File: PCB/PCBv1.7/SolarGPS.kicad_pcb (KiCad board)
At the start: 2 copper layers, 80 x 30 mm, 38 parts, among them J1 Conn_01x10_Female, J2 GND, J3 GND, J4 Solar1+, J5 Solar2+, J6 Conn_02x03_Odd_Even, J7 Screw_Terminal_01x01, J8 Conn_01x04_Male, SW1 SW_Push, U1 TPS63802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

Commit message: Submit board 1.7
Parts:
- removed D2: Schottky, Diode_SMD:D_SOD-323_HandSoldering
- added U5: LM66100, Package_TO_SOT_SMD:SOT-363_SC-70-6, F.Cu at (77.3, 55.0)
- added U6: LM66100, Package_TO_SOT_SMD:SOT-363_SC-70-6, F.Cu at (77.3, 52.1)
- D1: value Schottky -> 4V; footprint Diode_SMD:D_SOD-323_HandSoldering -> Diode_SMD:D_SMB_Handsoldering; moved to B.Cu
- U4: value MAX40200AUK -> LM66100; footprint Package_TO_SOT_SMD:SOT-23-5 -> Package_TO_SOT_SMD:SOT-363_SC-70-6
- moved D1 13.0 mm to (66.2, 61.5), turned to 90 degrees
- moved C10 1.88 mm to (73.0, 55.1)
- moved R4 0.72 mm to (116.0, 76.8)
- moved U4 0.30 mm to (116.0, 74.6)
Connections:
- net /VBAT renamed VBAT
- D1 pad 2: /SOLAR1+ -> GND
- U4 pad 5: /GPS_VDD -> GND
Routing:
- net VBAT: track 30.1 -> 46.4 mm
- net GND: vias 54 -> 55

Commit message: Tweak PCB
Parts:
- removed D1: 4V, Diode_SMD:D_SMB_Handsoldering
- removed R4: 432k, Resistor_SMD:R_0603_1608Metric
- removed SW1: SW_Push, Button_Switch_SMD:SW_SPST_CK_RS282G05A3
- added C11: 1uF, Capacitor_SMD:C_0603_1608Metric, F.Cu at (78.0, 70.9)
- added D3: LED_Small, Diode_SMD:D_0805_2012Metric, F.Cu at (57.3, 57.2)
- added R5: 60, Resistor_SMD:R_0603_1608Metric, F.Cu at (60.6, 57.5)
- added U7: MAX40200AUK, Package_TO_SOT_SMD:SOT-23-5, F.Cu at (107.3, 99.8)
- C7: value 0.1uF -> 1uF
- R1: value 100 -> 86k
- U4: value LM66100 -> BMI160; footprint Package_TO_SOT_SMD:SOT-363_SC-70-6 -> digikey-footprints:BMI160
- U5, U6: value LM66100 -> MAX40200AUK; footprint Package_TO_SOT_SMD:SOT-363_SC-70-6 -> Package_TO_SOT_SMD:SOT-23-5
- moved U6 60.1 mm to (107.3, 104.2), turned to 0 degrees
- moved U5 56.9 mm to (112.5, 99.8), turned to 0 degrees
- moved U4 38.8 mm to (77.2, 73.5), turned to 90 degrees
- moved C16 3.03 mm to (73.0, 69.3), turned to 90 degrees
- moved C1 1.05 mm to (118.8, 74.1)
- moved C5 0.98 mm to (119.0, 75.9)
- moved R6 0.25 mm to (63.8, 57.5)
- moved C7 0.20 mm to (63.5, 51.5)
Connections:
- C10 pad 2: VBAT -> /VBAT
- C4 pad 1: VBAT -> /VBAT
- C6 pad 2: VBAT -> /VBAT
- R2 pad 1: VBAT -> /VBAT
- U1 pad 10: VBAT -> /VBAT
- U3 pad 14: unconnected-(U3-Pad14) -> MMU_INT
- U3 pad 15: unconnected-(U3-Pad15) -> MMU_CS
- U3 pad 18: LCDEN -> SOLAREN
- U3 pad 19: DISPCS -> LCDEN
- U3 pad 20: unconnected-(U3-Pad20) -> DISPCS
- U3 pad 22: unconnected-(U3-Pad22) -> LED
- U3 pad 6: Button -> unconnected-(U3-Pad6)
- U4 pad 1: VDD -> SPI_MISO
- U4 pad 2: GND -> unconnected-(U4-Pad2)
- U4 pad 3: GPS_EN -> unconnected-(U4-Pad3)
- U4 pad 4: unconnected-(U4-Pad4) -> MMU_INT
- U4 pad 5: GND -> VDD
- U4 pad 6: /GPS_VDD -> GND
- U5 pad 1: /SOLAR1+ -> VDD
- U5 pad 3: VBAT -> GPS_EN
- U5 pad 5: GND -> /GPS_VDD
- U6 pad 1: /SOLAR2+ -> /SOLAR1+
- U6 pad 3: VBAT -> SOLAREN
- U6 pad 5: GND -> /VBAT
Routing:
- net VBAT: track 46.4 -> 0.00 mm, vias 1 -> 0
- net /VBAT: track 0.00 -> 36.4 mm, vias 0 -> 1
- net Button: track 28.3 -> 0.00 mm, vias 2 -> 0
- net LED: track 0.00 -> 20.9 mm
- net VDD: track 145.4 -> 164.6 mm, vias 3 -> 2
- net /GPS_VDD: track 17.6 -> 0.00 mm
- net MMU_INT: track 0.00 -> 13.0 mm, vias 0 -> 2
- net GPS_EN: track 47.5 -> 59.4 mm, vias 1 -> 3
- net SPI_CLK: track 15.7 -> 19.7 mm, vias 2 -> 3
- net MMU_CS: track 0.00 -> 3.97 mm
- net SPI_MISO: track 0.00 -> 3.96 mm
- net GND: track 7.95 -> 11.8 mm, vias 55 -> 59
- net SPI_MOSI: track 17.5 -> 19.7 mm
- net Net-(D3-Pad2): track 0.00 -> 1.69 mm

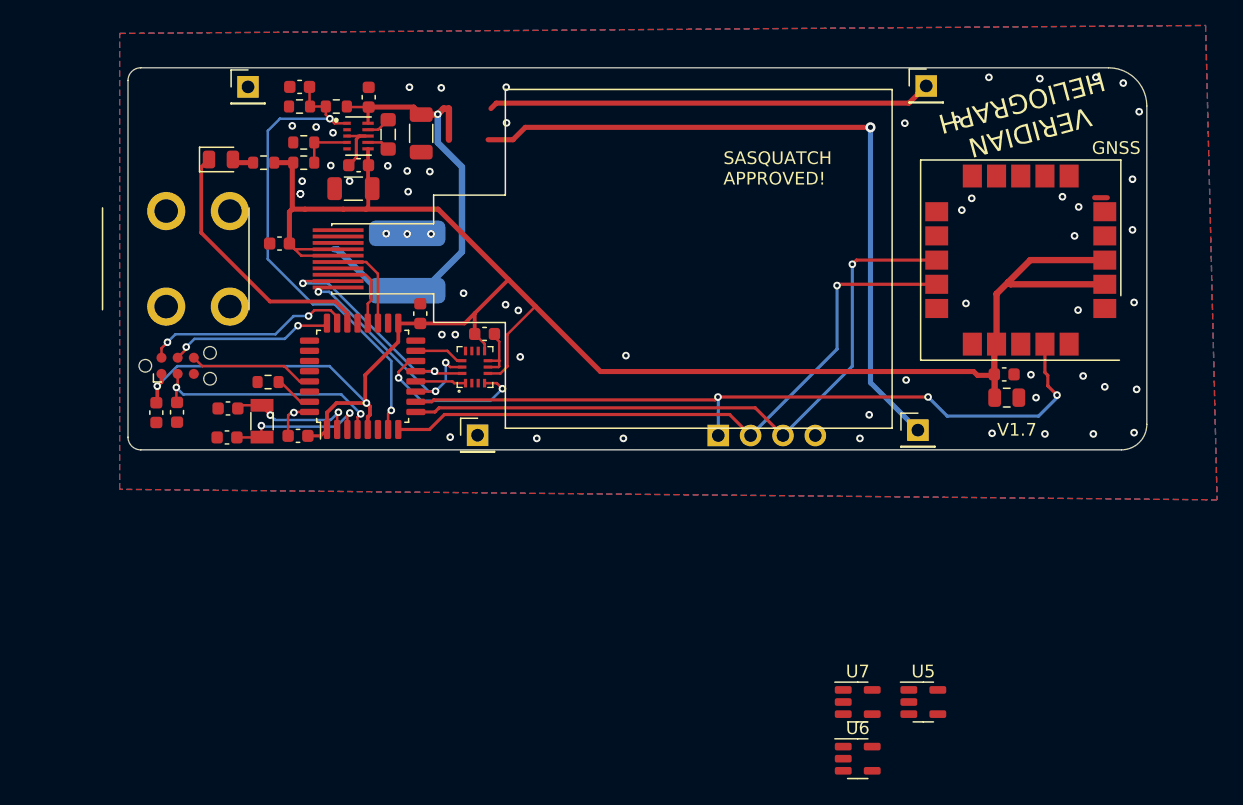
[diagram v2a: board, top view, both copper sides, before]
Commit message: add USB!
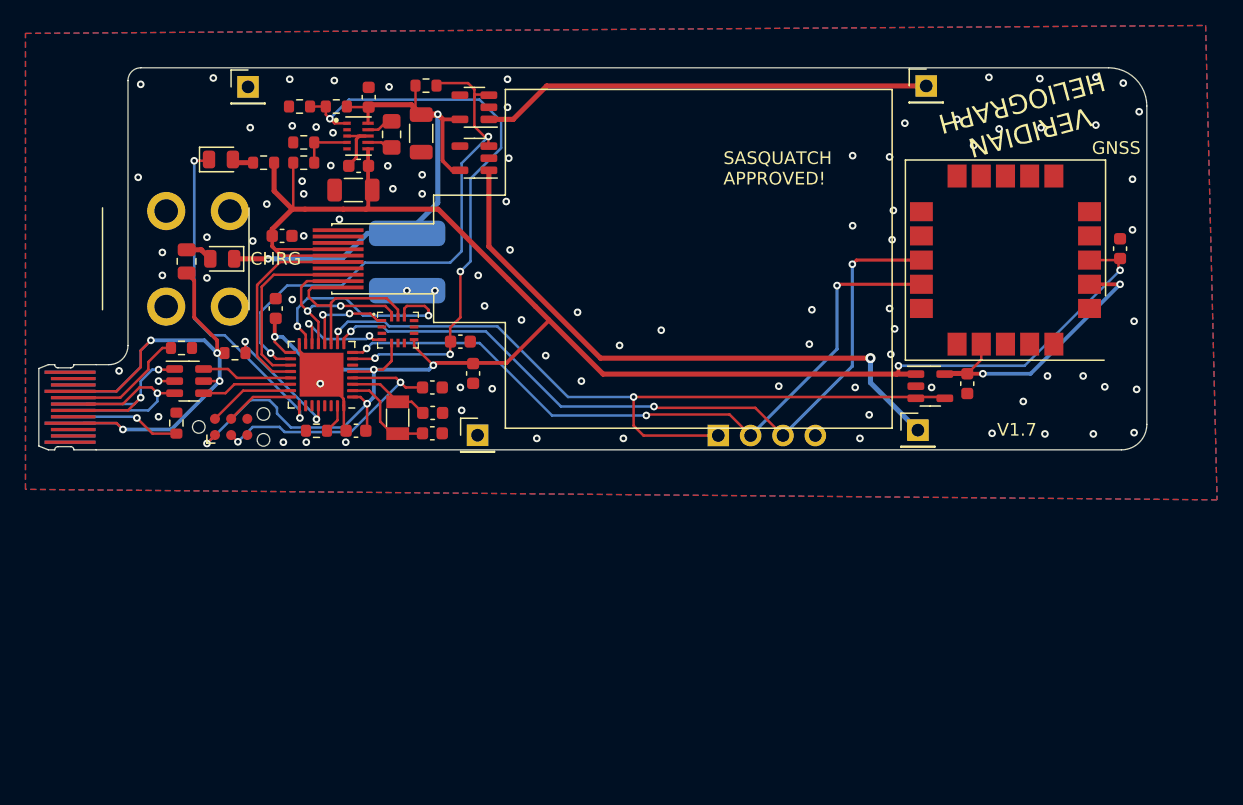
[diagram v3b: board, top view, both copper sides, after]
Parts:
- removed C11, C19: 1uF, Capacitor_SMD:C_0603_1608Metric
- removed C5: 4.7uF, Capacitor_SMD:C_0805_2012Metric
- added C12: 1uF, Capacitor_SMD:C_0603_1608Metric, F.Cu at (127.9, 64.2)
- added C17: 1uF, Capacitor_SMD:C_0603_1608Metric, F.Cu at (77.1, 74.0)
- added D1: LED_Small, Diode_SMD:D_0805_2012Metric, F.Cu at (57.4, 65.0)
- added J9: USB_C_Receptacle_USB2.0, Veridian:USB_TYPE_C_PCB, F.Cu at (43.0, 76.7)
- added R10: 10, Resistor_SMD:R_0805_2012Metric, F.Cu at (54.6, 65.2)
- added R11: 5.1K, Resistor_SMD:R_0603_1608Metric, F.Cu at (58.4, 72.4)
- added R4: 86k, Resistor_SMD:R_0603_1608Metric, F.Cu at (73.4, 51.4)
- added R8: 5.1K, Resistor_SMD:R_0603_1608Metric, F.Cu at (54.2, 72.0)
- added R9: 5.1K, Resistor_SMD:R_0603_1608Metric, F.Cu at (53.8, 77.9)
- added U8: USBLC6-2SC6, Package_TO_SOT_SMD:SOT-23-6, F.Cu at (54.8, 74.6)
- C10, C9: value 47uF -> 22uF
- C8: value 10nF -> 1uF
- L1: footprint Inductor_SMD:L_0805_2012Metric_Pad1.05x1.20mm_HandSolder -> Inductor_SMD:L_0805_2012Metric_Pad1.15x1.40mm_HandSolder
- U3: value STM32L071KBTx -> STM32L432KCUx; footprint Package_QFP:LQFP-32_7x7mm_P0.8mm -> Package_DFN_QFN:QFN-32-1EP_5x5mm_P0.5mm_EP3.45x3.45mm
- moved U6 55.9 mm to (77.2, 57.1), turned to 180 degrees
- moved U7 55.6 mm to (77.2, 53.1), turned to 180 degrees
- moved U5 24.8 mm to (113.0, 75.0)
- moved C7 23.6 mm to (76.1, 71.5), turned to 180 degrees
- moved C2 20.1 mm to (73.9, 75.1), turned to 0 degrees
- moved C13 16.3 mm to (73.9, 77.1), turned to 0 degrees
- moved C15 16.2 mm to (73.9, 78.7), turned to 0 degrees
- moved Y1 10.7 mm to (71.2, 77.5), turned to -90 degrees
- moved C16 10.5 mm to (67.9, 78.5), turned to 180 degrees
- moved C14 10.2 mm to (61.6, 68.9), turned to 90 degrees
- moved U4 6.71 mm to (71.2, 70.6), turned to 0 degrees
- moved J6 6.38 mm to (58.1, 78.2)
- moved R1 5.39 mm to (64.8, 78.5)
- moved U3 3.23 mm to (65.2, 74.1), turned to 180 degrees
- moved C1 2.99 mm to (115.9, 74.8), turned to 90 degrees
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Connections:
- net /VBAT renamed VBAT
- J6 pad 6: UART1TX -> unconnected-(J6-Pad6)
- U3 pad 19: LCDEN -> DISPCS
- U3 pad 20: DISPCS -> LCDEN
- U3 pad 21: unconnected-(U3-Pad21) -> USB_N
- U3 pad 22: LED -> USB_P
- U3 pad 25: unconnected-(U3-Pad25) -> LED
- U3 pad 28: unconnected-(U3-Pad28) -> Net-(U3-Pad28)
- U3 pad 29: UART1TX -> unconnected-(U3-Pad29)
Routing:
- net VUSB: track 0.00 -> 49.4 mm, vias 0 -> 4
- net SOLAREN: track 0.00 -> 42.6 mm, vias 0 -> 2
- net /GPS_VDD: track 0.00 -> 21.8 mm, vias 0 -> 2
- net USBR_P: track 0.00 -> 14.2 mm, vias 0 -> 1
- net USBR_N: track 0.00 -> 13.6 mm, vias 0 -> 2
- net MMU_CS: track 3.97 -> 17.5 mm, vias 0 -> 2
- net Net-(U3-Pad28): track 0.00 -> 10.5 mm, vias 0 -> 2
- net UART1TX: track 9.85 -> 0.00 mm
- net SWDIO: track 16.5 -> 6.85 mm, vias 2 -> 0
- net /SOLAR1+: track 55.7 -> 46.8 mm
- net Net-(J9-PadA5): track 0.00 -> 8.64 mm
- net LCDEN: track 7.38 -> 15.8 mm
- net DISPCS: track 6.26 -> 14.3 mm
- net GPS_UART_MISO: track 52.3 -> 60.1 mm, vias 1 -> 3
- net Net-(J9-PadB5): track 0.00 -> 7.65 mm, vias 0 -> 1
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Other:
- board size 80 x 30 mm -> 82.5 x 30 mm
- board text added: "CHRG"

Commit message: Add USB pulldown and SWO
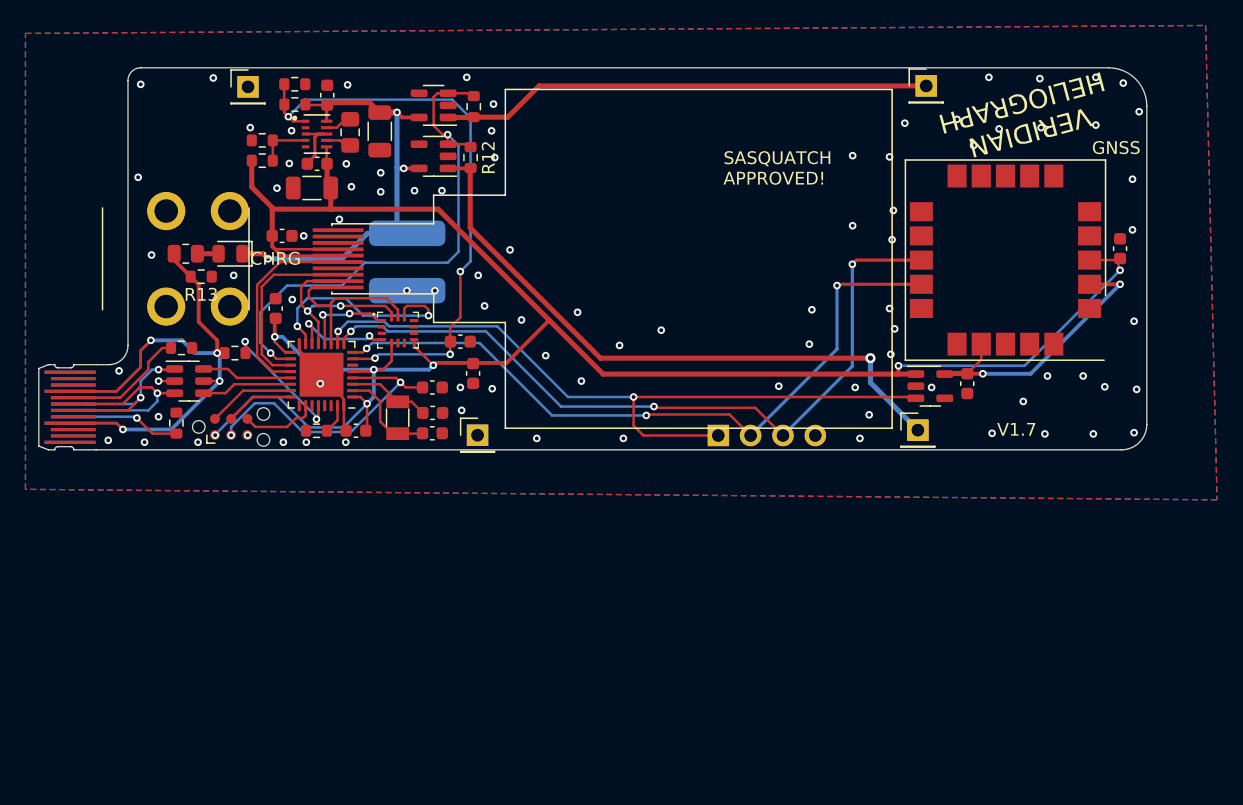
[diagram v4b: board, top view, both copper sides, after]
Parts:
- removed D3: LED_Small, Diode_SMD:D_0805_2012Metric
- removed R5: 60, Resistor_SMD:R_0603_1608Metric
- added R12: 86k, Resistor_SMD:R_0603_1608Metric, F.Cu at (76.9, 57.0)
- added R13: 5.1K, Resistor_SMD:R_0603_1608Metric, F.Cu at (55.8, 66.4)
- moved R4 4.10 mm to (77.2, 53.0), turned to -90 degrees
- moved C6 3.26 mm to (65.6, 52.1)
- moved C9 3.26 mm to (64.4, 59.4)
- moved C10 3.26 mm to (69.8, 55.0)
- moved L1 3.26 mm to (67.4, 55.1)
- moved R2 3.26 mm to (63.1, 52.9)
- moved C8 3.26 mm to (64.9, 57.5)
- moved R6 3.26 mm to (60.5, 57.3)
- moved R7 3.26 mm to (60.5, 55.7)
- moved U1 3.26 mm to (64.8, 55.2)
- moved U6 3.20 mm to (74.0, 57.0)
- moved U7 3.20 mm to (74.0, 53.0)
- moved R3 1.79 mm to (63.1, 51.3), turned to 0 degrees
- moved D1 0.76 mm to (58.0, 64.6)
- moved R10 0.60 mm to (54.5, 64.6), turned to 0 degrees
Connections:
- J6 pad 6: unconnected-(J6-Pad6) -> SWO
- R4 pad 2: VBAT -> /SOLAR2+
- U3 pad 26: unconnected-(U3-Pad26) -> SWO
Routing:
- net LED: track 26.5 -> 0.00 mm, vias 2 -> 0
- net VBAT: track 43.4 -> 36.8 mm, vias 2 -> 3
- net SWO: track 0.00 -> 5.98 mm
- net VDD: track 164.1 -> 159.9 mm
- net /SOLAR2+: track 35.4 -> 38.5 mm
- net GPS_EN: track 61.0 -> 58.4 mm
- net /SOLAR1+: track 46.8 -> 49.3 mm
- net VUSB: track 49.4 -> 51.4 mm
- net Net-(D3-Pad2): track 1.69 -> 0.00 mm
- net nRESET: track 21.6 -> 23.2 mm
- net SOLAREN: track 42.6 -> 42.0 mm
- net GND: vias 91 -> 88

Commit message: Do PCB 1.7
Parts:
- C4: value 25F -> 70F
- moved C4 5.94 mm to (69.5, 64.8)
- moved C17 1.24 mm to (75.9, 74.3)
- moved C7 0.46 mm to (75.7, 71.6)
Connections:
- J1 pad 4: unconnected-(J1-Pad4) -> EXTIN
- U3 pad 4: nRESET -> unconnected-(U3-Pad4)
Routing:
- net nRESET: track 23.2 -> 19.2 mm
- net VBAT: track 36.8 -> 33.7 mm
- net SOLAREN: track 42.0 -> 40.8 mm
- net MMU_CS: track 17.5 -> 16.5 mm
- net GPS_UART_MISO: track 60.1 -> 59.5 mm
- net GND: vias 88 -> 95
